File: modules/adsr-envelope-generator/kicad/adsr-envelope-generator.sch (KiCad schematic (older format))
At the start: 78 parts, among them P1 CONN_01X03, P2 CONN_01X02, P3 CONN_01X02, P4 CONN_01X03, Q1 Q_NPN_EBC, Q2 Q_NPN_EBC, Q3 Q_NPN_EBC, U1 TL074, U2 4066, U3 40106, U4 TL074, U5 4001

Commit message: [WiP] ADSR board layout
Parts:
- C1, C10, C11, C18, C19, C2, C20, C3, C4, C5, C7, C9: footprint (none) -> Capacitors_SMD:C_0805_HandSoldering
- C12, C13: footprint (none) -> Capacitors_ThroughHole:C_Radial_D8_L11.5_P3.5
- C14, C15, C16, C17, C6: footprint (none) -> SMD_Packages:SMD-1206_Pol
- C8: footprint (none) -> Capacitors_ThroughHole:C_Radial_D10_L13_P5
- D1, D2, D3, D4, D5, D6, D7, D8, D9: footprint (none) -> Diodes_SMD:SOD-323_HandSoldering
- P1, P4: footprint (none) -> Pin_Headers:Pin_Header_Straight_1x03
- P2, P3: footprint (none) -> Pin_Headers:Pin_Header_Straight_1x02
- Q1, Q2, Q3: footprint (none) -> TO_SOT_Packages_SMD:SOT-23_Handsoldering
- R1, R10, R11, R12, R13, R14, R15, R16, R17, R18, R19, R2, R20, R21, R22, R23, R24, R25, R26, R27, R28, R29, R3, R30, R31, R32, R33, R4, R5, R6, R7, R8, R9: footprint (none) -> Resistors_SMD:R_1206_HandSoldering
- RV1, RV2, RV3, RV4: footprint (none) -> Bourns PTL:Bourns PTL30-X
- U1, U2, U3, U4, U5: footprint (none) -> SMD_Packages:SOIC-14_N

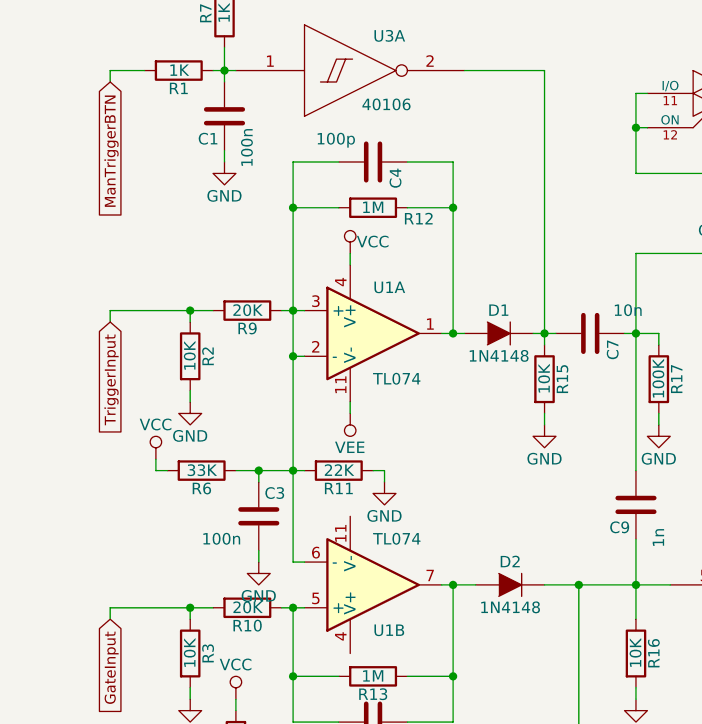
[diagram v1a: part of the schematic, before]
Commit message: Redo ADSR generator PCB layout
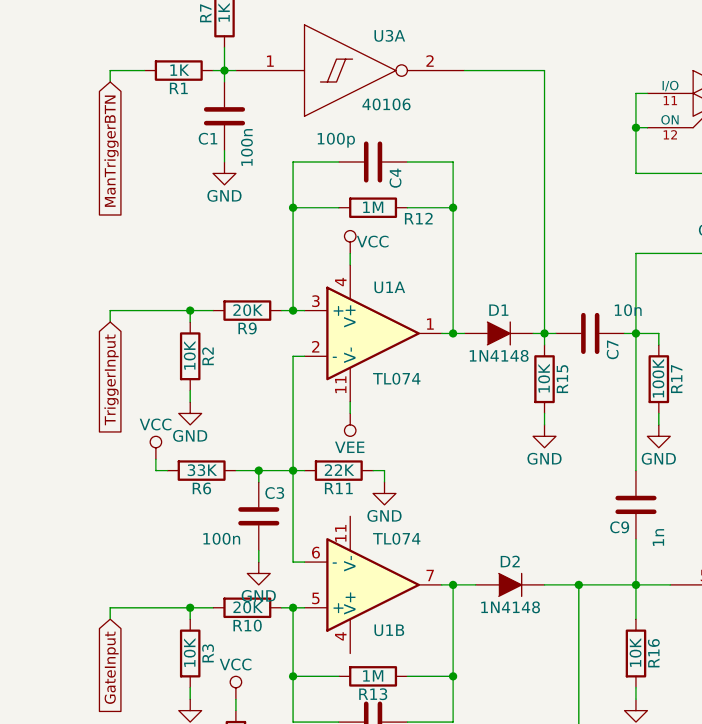
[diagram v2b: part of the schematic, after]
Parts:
- C12, C13: footprint Capacitors_ThroughHole:C_Radial_D8_L11.5_P3.5 -> Capacitors_ThroughHole:CP_Radial_D8.0mm_P3.80mm
- C8: footprint Capacitors_ThroughHole:C_Radial_D10_L13_P5 -> Capacitors_ThroughHole:CP_Radial_D10.0mm_P5.00mm
- D1, D2, D3, D4, D5, D6, D7, D8, D9: footprint Diodes_SMD:SOD-323_HandSoldering -> Diodes_SMD:SOD-323
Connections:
- net at C3.1, R11.2, R6.1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: no longer C4.2, R12.2, R9.1, U1.3 (+)
- new net: C4.2, R12.2, R9.1, U1.3 (+)

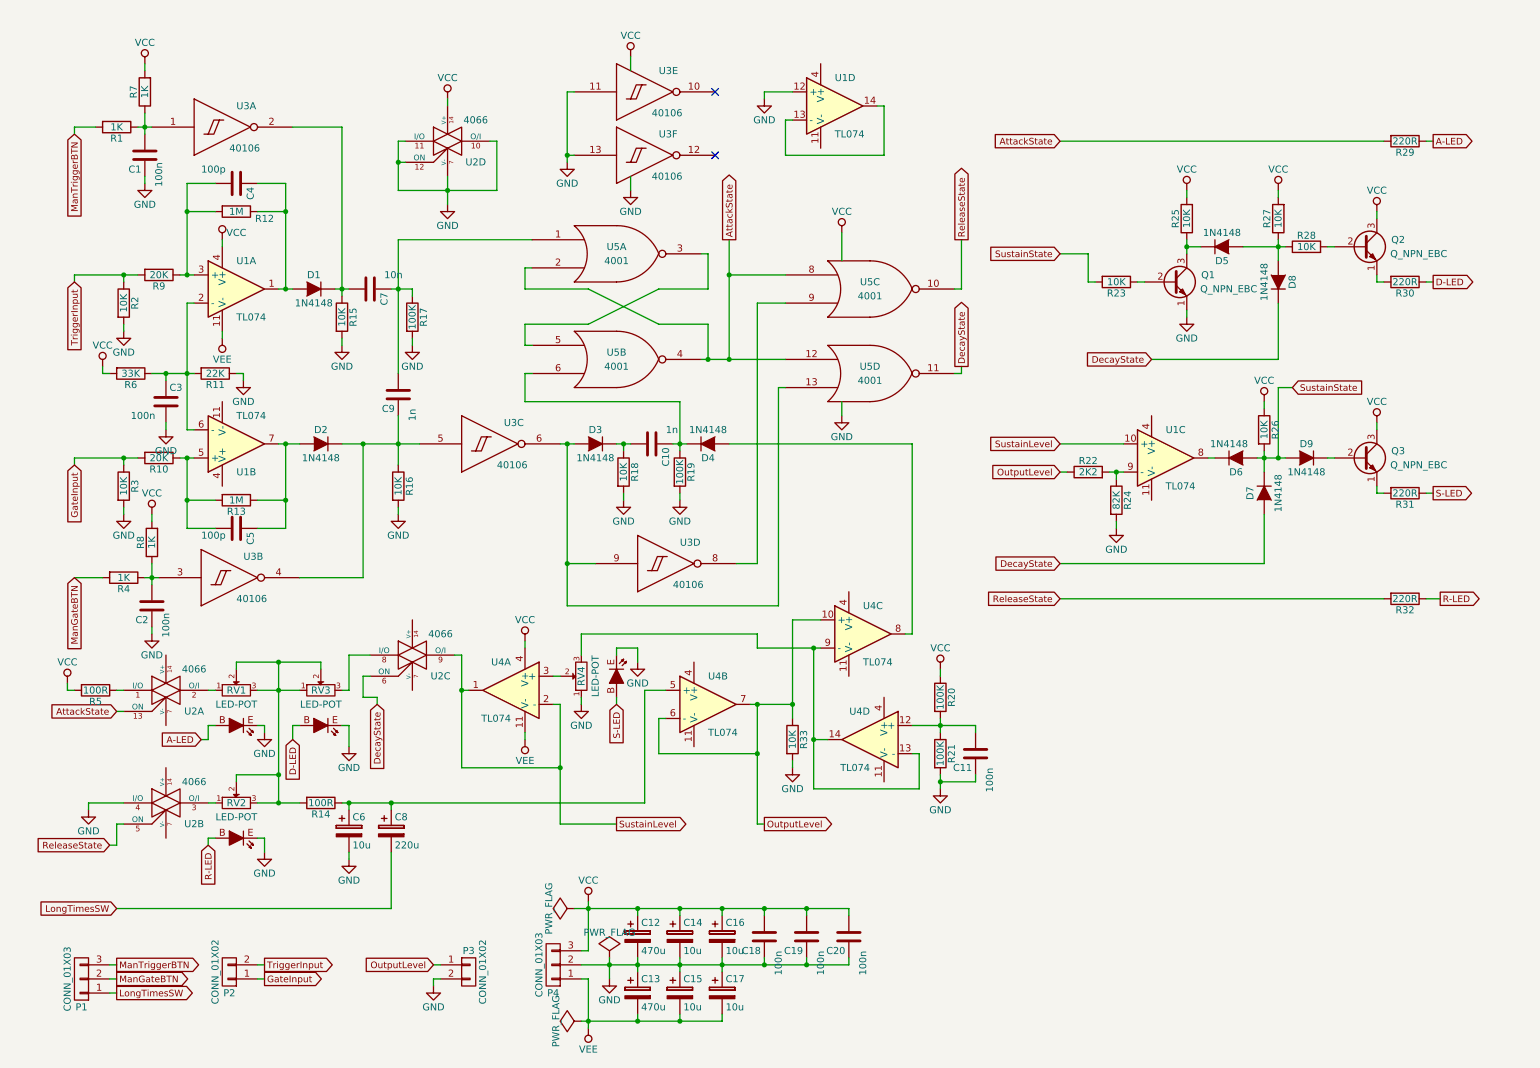
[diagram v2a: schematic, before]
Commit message: Finish up ADSR generator schematic, PCB, replace broken one
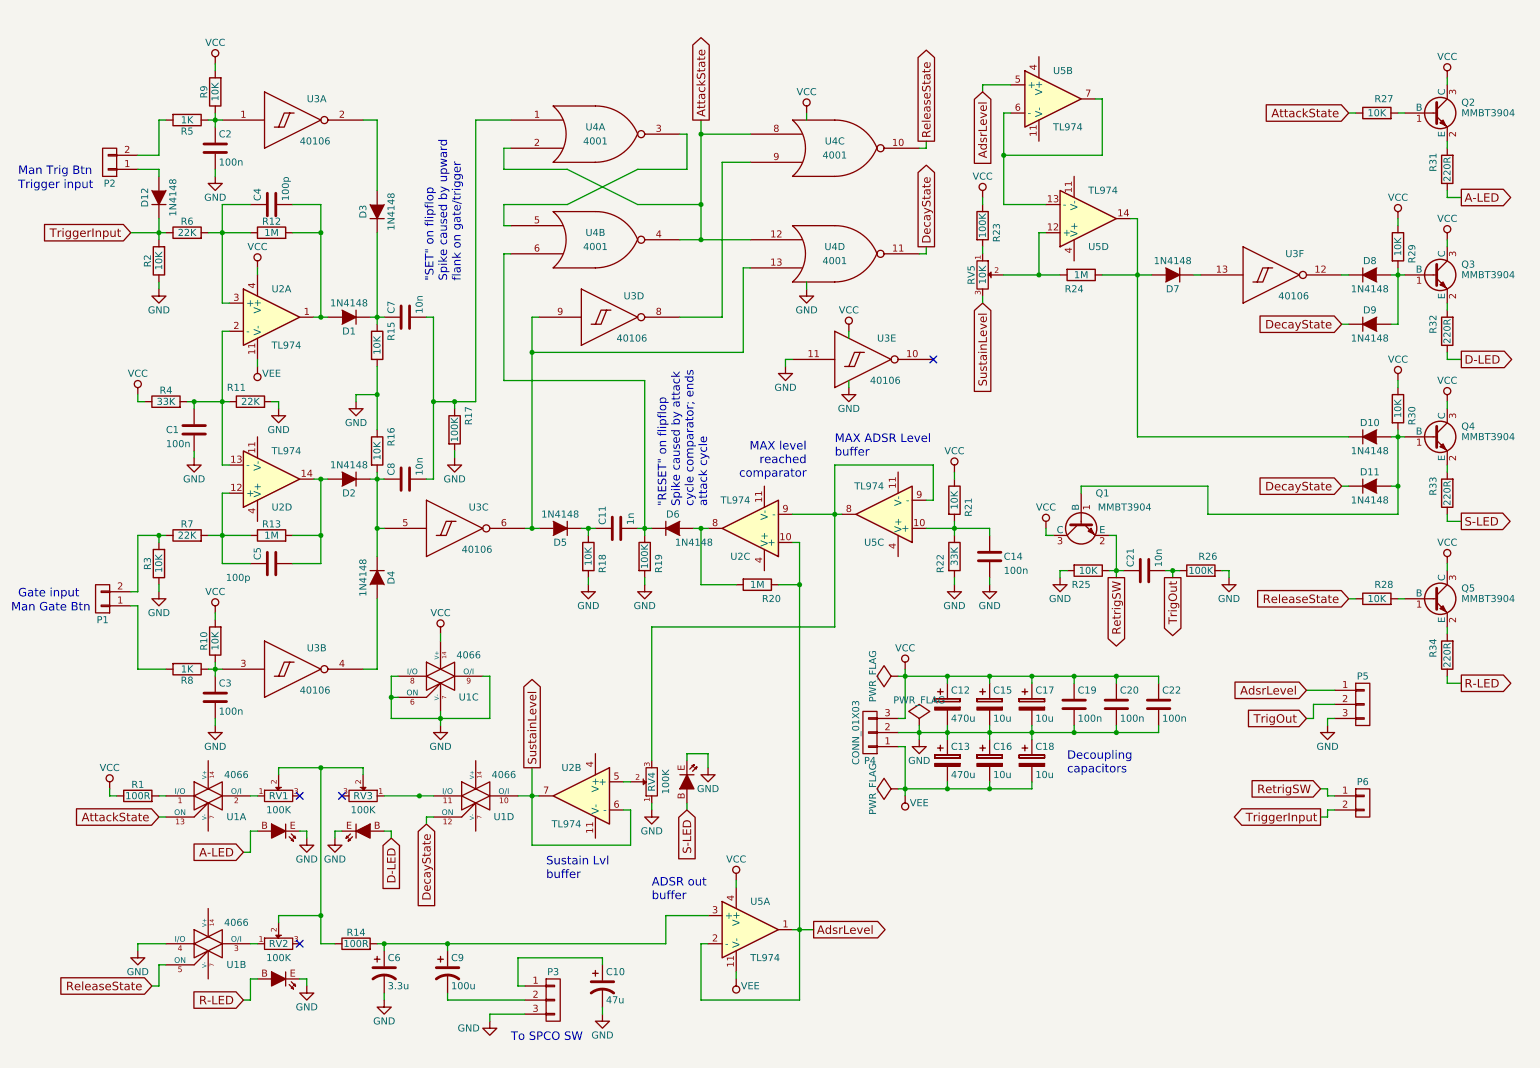
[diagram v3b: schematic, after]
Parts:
- removed C10, C9: 1n, Capacitors_SMD:C_0805_HandSoldering, symbol C
- removed C14, C6: 10u, SMD_Packages:SMD-1206_Pol, symbol CP
- removed C18: 100n, Capacitors_SMD:C_0805_HandSoldering, symbol C
- removed C8: 220u, Capacitors_ThroughHole:CP_Radial_D10.0mm_P5.00mm, symbol CP
- removed P1: CONN_01X03, Pin_Headers:Pin_Header_Straight_1x03, symbol CONN_01X03
- removed P3: CONN_01X02, Pin_Headers:Pin_Header_Straight_1x02, symbol CONN_01X02
- removed Q1, Q2, Q3: Q_NPN_EBC, TO_SOT_Packages_SMD:SOT-23_Handsoldering, symbol Q_NPN_EBC
- removed U1, U4: TL074, SMD_Packages:SOIC-14_N, symbol TL074
- removed U2: 4066, SMD_Packages:SOIC-14_N, symbol 4066
- removed U5: 4001, SMD_Packages:SOIC-14_N, symbol 4001
- added C10: 47u, Capacitors_ThroughHole:CP_Radial_D5.0mm_P2.00mm, symbol CP1
- added C14, C22: 100n, Capacitors_SMD:C_0805, symbol C
- added C18: 10u, SMD_Packages:SMD-1206_Pol, symbol CP
- added C21, C8: 10n, Capacitors_SMD:C_0805, symbol C
- added C6: 3.3u, Capacitors_ThroughHole:CP_Radial_D4.0mm_P1.50mm, symbol CP1
- added C9: 100u, Capacitors_ThroughHole:CP_Radial_D5.0mm_P2.00mm, symbol CP1
- added D10, D11, D12: 1N4148, Diodes_SMD:SOD-323, symbol D
- added P1, P6: CONN_01X02, Pin_Headers:Pin_Header_Straight_1x02_Pitch2.54mm, symbol CONN_01X02
- added P3, P5: CONN_01X03, Pin_Headers:Pin_Header_Straight_1x03_Pitch2.54mm, symbol CONN_01X03
- added Q1, Q2, Q3, Q4, Q5: MMBT3904, TO_SOT_Packages_SMD:SOT-23, symbol MMBT3904
- added R34: 220R, Resistors_SMD:R_0805, symbol R
- added RV5: 10K, Potentiometers:Potentiometer_Triwood_RM-065, symbol POT
- added U1: 4066, SMD_Packages:SOIC-14_N, symbol 4066
- added U2, U5: TL974, SMD_Packages:SOIC-14_N, symbol TL074
- added U4: 4001, SMD_Packages:SOIC-14_N, symbol 4001
- C1, C19, C2, C20, C3, C4, C5, C7: footprint Capacitors_SMD:C_0805_HandSoldering -> Capacitors_SMD:C_0805
- C11: value 100n -> 1n; footprint Capacitors_SMD:C_0805_HandSoldering -> Capacitors_SMD:C_0805
- C12, C13: footprint Capacitors_ThroughHole:CP_Radial_D8.0mm_P3.80mm -> Capacitors_ThroughHole:CP_Radial_D8.0mm_P3.50mm
- P2: footprint Pin_Headers:Pin_Header_Straight_1x02 -> Pin_Headers:Pin_Header_Straight_1x02_Pitch2.54mm
- P4: footprint Pin_Headers:Pin_Header_Straight_1x03 -> Pin_Headers:Pin_Header_Straight_1x03_Pitch2.54mm
- R1: value 1K -> 100R; footprint Resistors_SMD:R_1206_HandSoldering -> Resistors_SMD:R_0805
- R10, R9: value 20K -> 10K; footprint Resistors_SMD:R_1206_HandSoldering -> Resistors_SMD:R_0805
- R11, R12, R13, R14, R15, R16, R17, R18, R19, R2, R25, R27, R28, R3, R31, R32, R8: footprint Resistors_SMD:R_1206_HandSoldering -> Resistors_SMD:R_0805
- R20: value 100K -> 1M; footprint Resistors_SMD:R_1206_HandSoldering -> Resistors_SMD:R_0805
- R21: value 100K -> 10K; footprint Resistors_SMD:R_1206_HandSoldering -> Resistors_SMD:R_0805
- R22: value 2K2 -> 33K; footprint Resistors_SMD:R_1206_HandSoldering -> Resistors_SMD:R_0805
- R23, R26: value 10K -> 100K; footprint Resistors_SMD:R_1206_HandSoldering -> Resistors_SMD:R_0805
- R24: value 82K -> 1M; footprint Resistors_SMD:R_1206_HandSoldering -> Resistors_SMD:R_0805
- R29, R30: value 220R -> 10K; footprint Resistors_SMD:R_1206_HandSoldering -> Resistors_SMD:R_0805
- R33: value 10K -> 220R; footprint Resistors_SMD:R_1206_HandSoldering -> Resistors_SMD:R_0805
- R4: value 1K -> 33K; footprint Resistors_SMD:R_1206_HandSoldering -> Resistors_SMD:R_0805
- R5: value 100R -> 1K; footprint Resistors_SMD:R_1206_HandSoldering -> Resistors_SMD:R_0805
- R6: value 33K -> 22K; footprint Resistors_SMD:R_1206_HandSoldering -> Resistors_SMD:R_0805
- R7: value 1K -> 22K; footprint Resistors_SMD:R_1206_HandSoldering -> Resistors_SMD:R_0805
- RV1, RV2, RV3, RV4: value LED-POT -> 100K; footprint Bourns PTL:Bourns PTL30-X -> Bourns PTL:Bourns-PTL30-X
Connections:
- net A-LED: now also R31.1; no longer R29.1
- net AttackState: now also R27.1, U1.13 (ON), U4.12, U4.2, U4.4, U4.8; no longer R29.2
- net D-LED: now also R32.1; no longer R30.1
- net DecayState: now also D9.1 (K), D11.1 (K), U1.12 (ON), U4.11; no longer D7.2 (A), D8.1 (K)
- net GND: now also C1.2, C15.2, C16.1, C17.2, C19.2, C2.2, C20.2, R11.2, R16.1, R2.1, R22.2, R25.2, R26.2, R3.1, C10.2, C14.2, C18.1, C22.2, C6.2, P3.3 (P3), P5.3 (P3), U1.4 (I/O), U1.6 (ON), U1.7 (V-), U1.8 (I/O), U1.9 (O/I), U4.7 (VSS), U4.7 (VSS), U4.7 (VSS), U4.7 (VSS); no longer C1.1, C11.1, C15.1, C16.2, C17.1, C19.1, C2.1, C20.1, R11.1, R16.2, R2.2, R21.2, R24.2, R3.2, R33.2, U3.13 (In)
- net R-LED: now also R34.1; no longer R32.1
- net ReleaseState: now also R28.1, U1.5 (ON), U4.10; no longer R32.2
- net S-LED: now also R33.1; no longer R31.1
- net SustainLevel: now also RV5.3, U1.10 (O/I), U2.6 (-), U2.7
- net TriggerInput: now also R2.2, R6.1, D12.1 (K), P6.2 (P2); no longer P2.2 (P2), R2.1, R9.2
- net VCC: now also C15.1, C17.1, C19.1, C20.1, R1.1, R10.2, R21.1, R23.1, R29.1, R30.1, R4.1, R9.2, C22.1, Q1.3 (C), Q2.3 (C), Q3.3 (C), Q4.3 (C), Q5.3 (C), U1.14 (V+), U2.4 (V+), U4.14 (VDD), U4.14 (VDD), U4.14 (VDD), U4.14 (VDD), U5.4 (V+); no longer C16.1, C19.2, C20.2, R20.1, R25.2, R26.1, R27.2, R5.2, R6.2, R7.2, R8.2
- net VEE: now also C16.2, C18.2, U2.11 (V-), U5.11 (V-); no longer C15.2, C17.2
- net at C4.1, R12.1: now also R6.2, U2.3 (+); no longer D1.2 (A)
- net at C4.2, R12.2: now also D1.2 (A), U2.1; no longer R9.1
- net at C5.2, R13.2: now also D2.2 (A), U2.14; no longer R10.1
- net at C5.1, R13.1: now also R7.2, U2.12 (+); no longer D2.2 (A)
- net at D6.1 (K): now also C11.2, R19.1, U4.6
- net at R24.1: now also D7.2 (A), D10.1 (K), U5.14; no longer R22.2
- net at D1.1 (K), R15.1: now also C7.1, D3.1 (K); no longer C7.2, U3.2 (Out)
- net at D2.1 (K), U3.5 (In): now also D4.1 (K), R16.2, C8.1; no longer R16.1, U3.4 (Out)
- net at R17.1: now also C7.2, C8.2, U4.1; no longer C7.1
- net at R8.1, U3.3 (In): now also C3.1, R10.1; no longer C2.2, R4.1
- net at U3.6 (Out), U3.9 (In): now also D5.2 (A), U4.13; no longer D3.2 (A)
- net at R18.1: now also C11.1, D5.1 (K); no longer D3.1 (K)
- net at U3.8 (Out): now also U4.9
- net at R5.1: now also C2.1, R9.1, U3.1 (In)
- net at RV1.1: now also U1.2 (O/I)
- net at RV2.1: now also U1.3 (O/I)
- net at R14.1: now also RV1.2, RV2.2, RV3.2
- net at RV4.2: now also U2.5 (+)
- net at RV4.3: now also U2.9 (-), U5.8, U5.9 (-)
- net at D4.2 (A): now also U3.4 (Out)
- net RetrigSW: now reaches R25.1
- net RetrigSW: now also C21.1, P6.1 (P1), Q1.2 (E); no longer D5.1 (K)
- net at R28.2: now also Q5.1 (B)
- net at R30.2: now also D10.2 (A), D11.2 (A), Q1.1 (B), Q4.1 (B)
- net at R31.2: now also Q2.2 (E)
- net at U3.12 (Out): now also D8.1 (K)
- removed net GateInput: P2.1 (P1), R10.2, R3.1
- net ManGateBTN: no longer names the net of R4.2
- net ManGateBTN: now also C1.1, R11.1, U2.13 (-), U2.2 (-)
- net ManTriggerBTN: no longer names the net of R1.2
- net ManTriggerBTN: now also U1.1 (I/O)
- net OutputLevel: no longer names the net of R22.1
- net OutputLevel: now also R21.2, C14.1, U5.10 (+); no longer R33.1
- removed net SustainState: D6.2 (A), D7.1 (K), D9.2 (A), R23.2, R26.2
- new net: P2.2 (P2), R5.2
- new net: P1.1 (P1), R8.2
- new net: D3.2 (A), U3.2 (Out)
- new net: P1.2 (P2), R3.2, R7.1
- new net: D6.2 (A), R20.2, U2.8
- new net: C6.1, C9.1, R14.2, U5.3 (+)
- new net: U4.3, U4.5
- new net: RV3.1, U1.11 (I/O)
- new net: C9.2, P3.2 (P2)
- new net: C10.1, P3.1 (P1)
- new net: U5.13 (-), U5.6 (-), U5.7
- new net: R23.2, RV5.1
- new net: R24.2, RV5.2, U5.12 (+)
- new net: Q2.1 (B), R27.2
- new net: D8.2 (A), D9.2 (A), Q3.1 (B), R29.2
- new net: Q3.2 (E), R32.2
- new net: Q4.2 (E), R33.2
- new net: Q5.2 (E), R34.2
- new net: D7.1 (K), U3.13 (In)
- new net: D12.2 (A), P2.1 (P1)
- new net AdsrLevel: P5.1 (P1), R20.1, U2.10 (+), U5.1, U5.2 (-), U5.5 (+)
- new net TrigOut: C21.2, P5.2 (P2), R26.1
- now unconnected: RV1.3, RV2.3
- no-connect marks 2 -> 4
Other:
- note added: ""RESET" on flipflop\nSpike caused by attack\ncycle comparator; ends\nattack cycle"
- note added: ""SET" on flipflop\nSpike caused by upward\nflank on gate/trigger"
- note added: "ADSR out\nbuffer"
- note added: "Decoupling\ncapacitors"
- note added: "Gate input"
- note added: "MAX ADSR Level\nbuffer"
- note added: "MAX level\nreached\ncomparator"
- note added: "Man Gate Btn"
- note added: "Man Trig Btn"
- note added: "Sustain Lvl\nbuffer"
- note added: "To SPCO SW"
- note added: "Trigger input"
